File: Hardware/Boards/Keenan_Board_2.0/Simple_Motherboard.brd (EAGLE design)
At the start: 146.1 x 133.3 mm, 100 parts, among them U1 WIZ811MJ, U1_MUX 74HC4052D,653, U2_MUX 74HC4052D,653, U3_MUX 74HC4052D,653, U4_MUX 74HC4052D,653, U5_MUX 74HC4052D,653, U7_MUX 74HC4052D,653

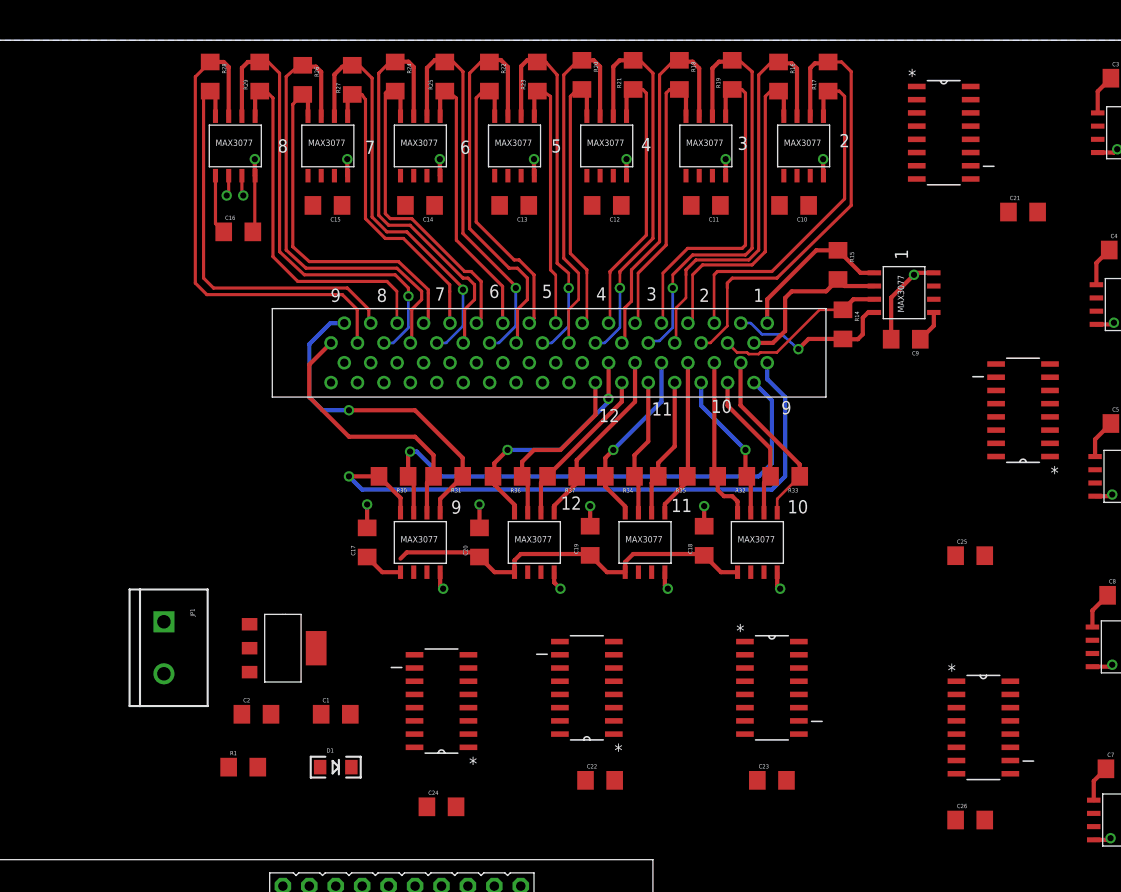
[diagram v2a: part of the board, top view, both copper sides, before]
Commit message: Routing power work
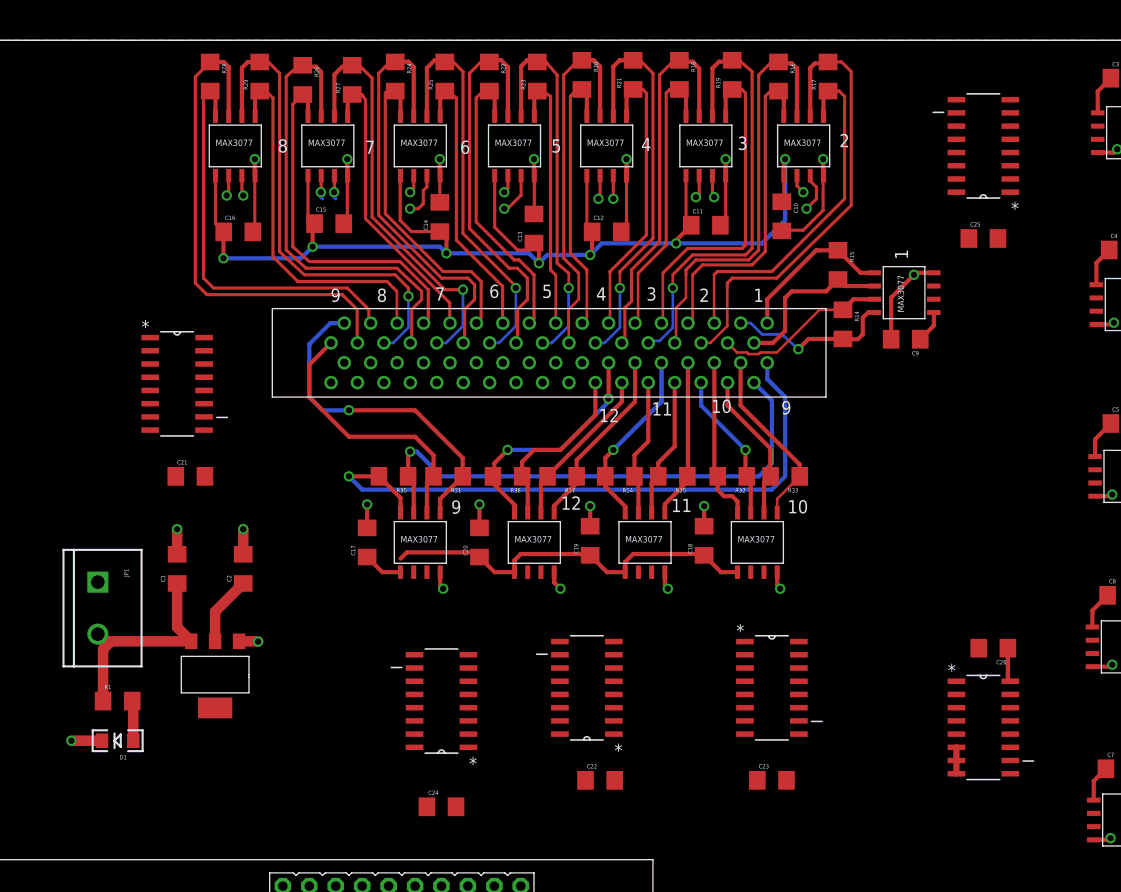
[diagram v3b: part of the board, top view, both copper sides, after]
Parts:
- moved C21 83.9 mm to (30.5, 91.4)
- moved U1_MUX 77.5 mm to (29.2, 100.3)
- moved C25 30.5 mm to (106.7, 114.3)
- moved U5_MUX 25.7 mm to (106.7, 123.2)
- moved D1 21.1 mm to (23.5, 66.0), turned to 180 degrees
- moved C1 20.7 mm to (29.2, 82.5), turned to 90 degrees
- moved C26 16.7 mm to (107.6, 74.9), turned to 180 degrees
- moved C2 14.0 mm to (35.6, 82.5), turned to 90 degrees
- moved R1 13.6 mm to (23.5, 69.8)
- moved JP1 7.41 mm to (21.6, 81.3)
- moved U$1 6.99 mm to (32.9, 72.4), turned to 180 degrees
- moved C13 2.93 mm to (63.5, 115.3), turned to 90 degrees
- moved C12 2.54 mm to (70.5, 114.9), turned to 0 degrees
- moved C14 2.21 mm to (54.5, 116.4), turned to 90 degrees
- moved C11 1.91 mm to (80.0, 115.6), turned to 0 degrees
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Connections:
- net +3V3: no longer R1.1
- net +5V: now also R1.1, U7_MUX.16
- net VCC: no longer U7_MUX.16
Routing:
- net +5V: track 72.1 -> 212.5 mm, vias 0 -> 7
- net GND: track 65.0 -> 108.1 mm, vias 28 -> 32
- net +3V3: track 0.00 -> 6.68 mm
- net RS485_6_TX: track 0.00 -> 4.31 mm, vias 0 -> 1
- net RS485_5_TX: track 0.00 -> 4.03 mm, vias 0 -> 1
- net N$45: track 0.00 -> 3.85 mm
- net RS485_2_TX: track 0.00 -> 3.82 mm, vias 0 -> 1
- net RS485_7_TX: track 0.00 -> 2.30 mm, vias 0 -> 1
- net RS485_7_RX: track 0.00 -> 2.30 mm, vias 0 -> 1
- net RS485_4_RX: track 0.00 -> 2.29 mm, vias 0 -> 1
- net RS485_4_TX: track 0.00 -> 2.22 mm, vias 0 -> 1
- net RS485_3_RX: track 0.00 -> 2.20 mm, vias 0 -> 1
- net RS485_3_TX: track 0.00 -> 2.13 mm, vias 0 -> 1
- net RS485_2_RX: track 0.00 -> 1.84 mm, vias 0 -> 1
- net RS485_5_RX: track 0.00 -> 1.73 mm, vias 0 -> 1
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
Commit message: More routing
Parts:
- moved C23 12.0 mm to (87.5, 74.1), turned to 180 degrees
- moved C21 11.9 mm to (30.8, 103.3), turned to 180 degrees
- moved U1_MUX 3.81 mm to (29.2, 96.5)
- moved U3_MUX 3.81 mm to (86.4, 67.3)
- moved C24 3.72 mm to (53.3, 63.2)
- moved C22 3.50 mm to (67.2, 64.5)
- moved C25 2.07 mm to (105.6, 116.0)
- moved C26 1.00 mm to (108.0, 74.0)
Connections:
- removed net VCC: U2_MUX.16, U3_MUX.16, U4_MUX.16, U5_MUX.16
- net +5V: now also U2_MUX.16, U3_MUX.16, U4_MUX.16, U5_MUX.16
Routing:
- net GND: track 108.1 -> 144.0 mm, vias 32 -> 44
- net +5V: track 212.5 -> 223.7 mm

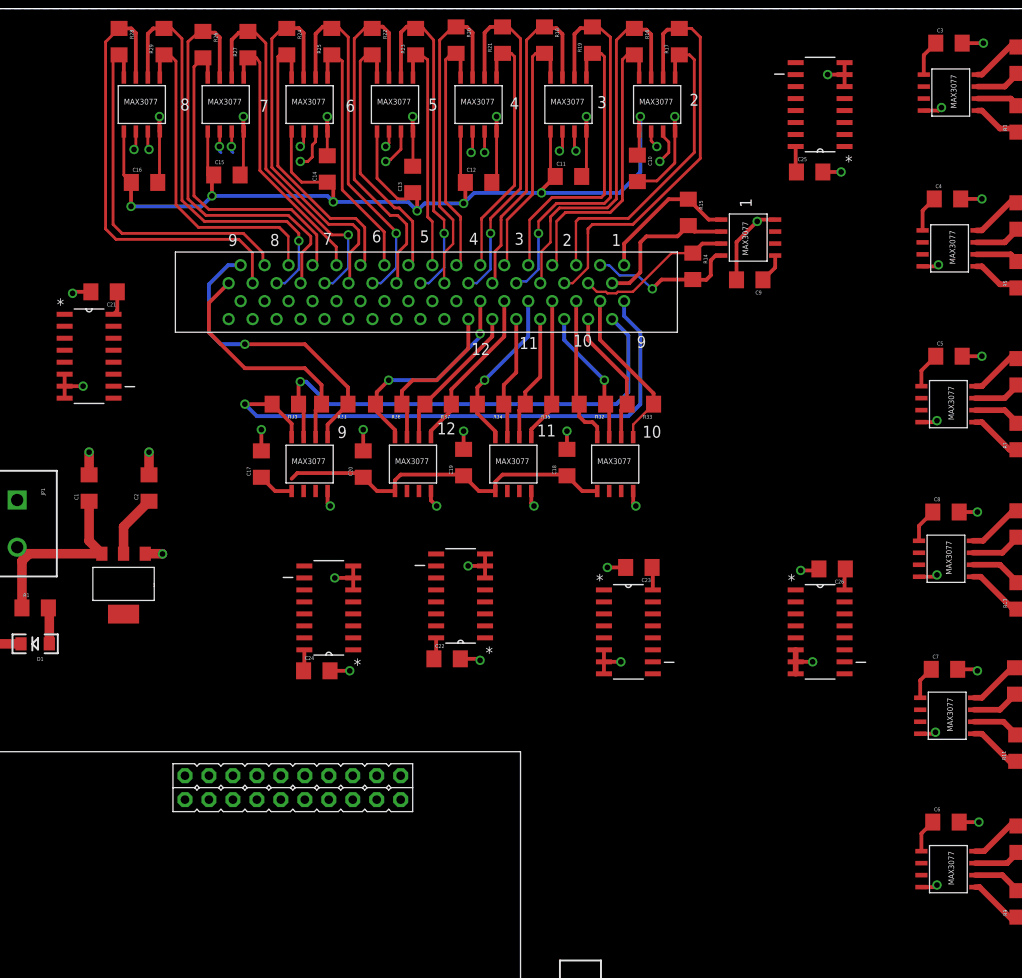
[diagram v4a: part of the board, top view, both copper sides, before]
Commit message: Routed some more mux stuff
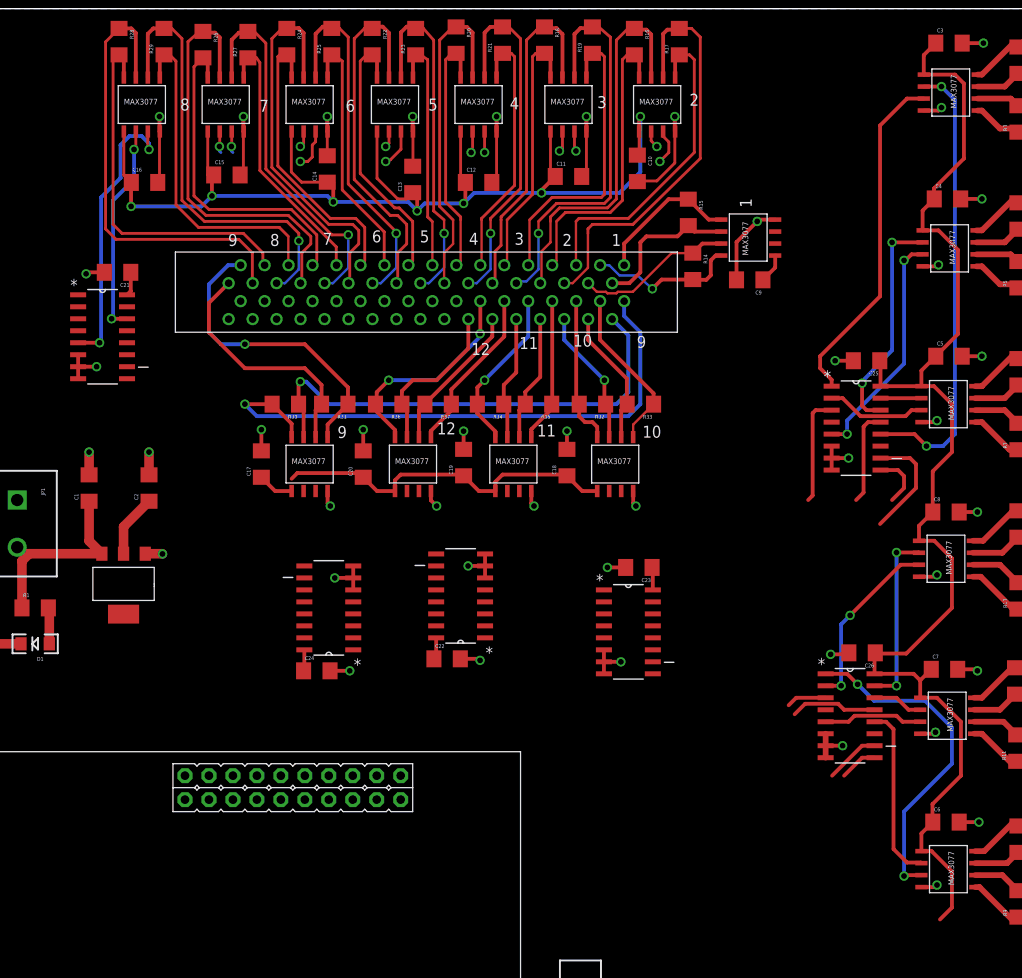
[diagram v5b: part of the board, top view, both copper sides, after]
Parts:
- moved U5_MUX 34.5 mm to (110.5, 88.9), turned to 0 degrees
- moved C25 20.9 mm to (111.6, 96.0), turned to 180 degrees
- moved C26 9.44 mm to (111.1, 65.1)
- moved U7_MUX 9.44 mm to (109.9, 58.4)
- moved C21 2.51 mm to (32.2, 105.4)
- moved U1_MUX 2.51 mm to (30.6, 98.6)
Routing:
- net +5V: track 223.7 -> 331.1 mm
- net RS485_13_RX: track 0.00 -> 48.2 mm, vias 0 -> 2
- net RS485_13_TX: track 0.00 -> 36.6 mm
- net RS485_16_TX: track 0.00 -> 35.5 mm, vias 0 -> 2
- net RS485_8_TX: track 1.96 -> 30.5 mm, vias 1 -> 2
- net RS485_14_TX: track 0.00 -> 24.8 mm, vias 0 -> 2
- net RS485_14_RX: track 0.00 -> 24.0 mm, vias 0 -> 2
- net RS485_8_RX: track 1.98 -> 22.5 mm, vias 1 -> 2
- net RS485_18_TX: track 0.00 -> 19.0 mm, vias 0 -> 2
- net RS485_18_RX: track 0.00 -> 18.9 mm, vias 0 -> 2
- net RS485_16_RX: track 0.00 -> 18.6 mm
- net U5_MUX_S0: track 0.00 -> 12.0 mm
- net U5TX: track 0.00 -> 11.5 mm
- net RS485_15_TX: track 0.00 -> 10.6 mm
- net RS485_17_TX: track 0.00 -> 10.5 mm
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
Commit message: Route city
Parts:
- moved S1 25.7 mm to (102.9, 40.6)
- moved U$2 16.6 mm to (25.4, 2.54)
- moved D1 13.8 mm to (32.5, 55.6)
- moved JP1 13.8 mm to (30.6, 70.8)
- moved U$1 13.8 mm to (41.9, 61.9)
- moved R1 13.8 mm to (32.5, 59.4)
- moved C1 13.8 mm to (38.3, 72.1)
- moved C2 13.8 mm to (44.6, 72.1)
- moved C23 12.7 mm to (90.3, 61.8), turned to 0 degrees
- moved U2_MUX 6.84 mm to (74.9, 68.6)
- moved C22 6.84 mm to (73.5, 61.9)
- moved U3_MUX 5.24 mm to (91.4, 68.6), turned to 180 degrees
- moved C18 5.08 mm to (84.9, 85.2)
- moved C19 5.08 mm to (74.0, 85.2)
- moved R15 5.08 mm to (97.8, 111.8)
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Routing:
- net RS485_5_RX: track 1.73 -> 132.2 mm, vias 1 -> 2
- net RS485_5_TX: track 4.03 -> 116.4 mm
- net RS485_1_TX: track 0.00 -> 105.1 mm, vias 0 -> 2
- net RS485_6_RX: track 1.73 -> 100.9 mm
- net RS485_6_TX: track 4.31 -> 101.8 mm
- net RS485_4_RX: track 2.29 -> 95.6 mm
- net RS485_1_RX: track 0.00 -> 91.0 mm, vias 0 -> 2
- net RS485_4_TX: track 2.22 -> 92.0 mm
- net RS485_7_TX: track 2.30 -> 87.4 mm
- net RS485_7_RX: track 2.30 -> 82.5 mm
- net RS485_3_RX: track 2.20 -> 81.3 mm
- net RS485_3_TX: track 2.13 -> 77.1 mm
- net RS485_2_RX: track 1.84 -> 65.2 mm
- net RS485_2_TX: track 3.82 -> 66.2 mm
- net +5V: track 331.1 -> 372.6 mm, vias 7 -> 13
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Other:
- board size 146.1 x 133.3 mm -> 120.7 x 133.3 mm
- board text removed: "Today, Tomorrow, Forever"

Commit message: All I do is route
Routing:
- net RS485_4_RX: track 95.6 -> 179.9 mm, vias 1 -> 2
- net RS485_4_TX: track 92.0 -> 163.5 mm, vias 1 -> 2
- net RS485_6_RX: track 100.9 -> 165.1 mm, vias 1 -> 2
- net RS485_6_TX: track 101.8 -> 160.8 mm, vias 1 -> 2
- net RS485_2_TX: track 66.2 -> 120.6 mm, vias 1 -> 2
- net RS485_2_RX: track 65.2 -> 112.7 mm, vias 1 -> 2
- net +5V: track 372.6 -> 419.1 mm
- net RS485_7_TX: track 87.4 -> 132.1 mm, vias 1 -> 2
- net RS485_7_RX: track 82.5 -> 121.4 mm, vias 1 -> 2
- net GND: track 144.7 -> 180.9 mm, vias 44 -> 48
- net RS485_3_RX: track 81.3 -> 113.4 mm, vias 1 -> 2
- net RS485_3_TX: track 77.1 -> 108.6 mm, vias 1 -> 2
- net RS485_10_RX: track 0.00 -> 31.0 mm, vias 0 -> 2
- net U5_MUX_S1: track 5.82 -> 33.1 mm
- net RS485_11_TX: track 0.00 -> 27.3 mm
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
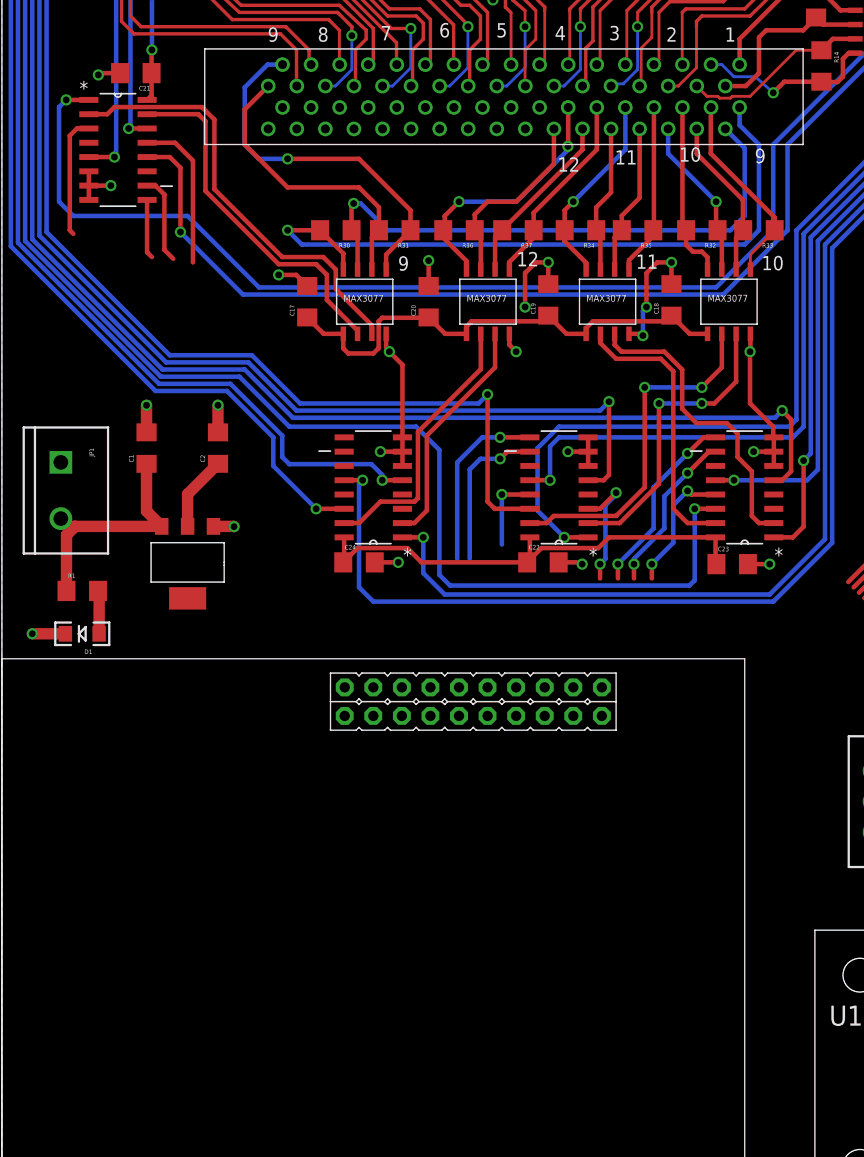
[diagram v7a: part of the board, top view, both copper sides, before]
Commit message: Basically just the breakout connections left
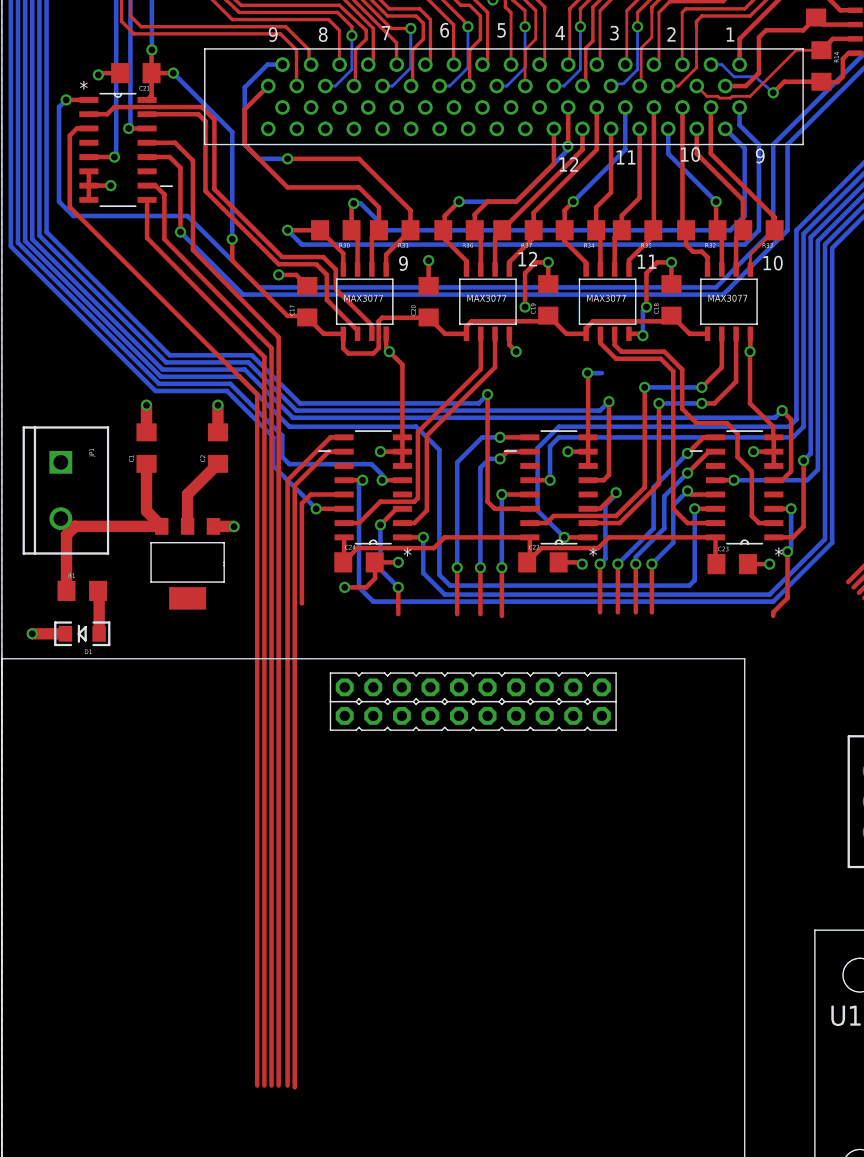
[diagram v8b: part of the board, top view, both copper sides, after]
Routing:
- net U1TX: track 10.8 -> 93.3 mm
- net U1_MUX_S1: track 5.26 -> 83.0 mm
- net U1_MUX_S0: track 7.91 -> 85.0 mm
- net U1RX: track 13.8 -> 90.1 mm
- net U4_MUX_S1: track 0.00 -> 60.4 mm
- net U4_MUX_S0: track 0.00 -> 59.1 mm
- net +5V: track 419.1 -> 448.7 mm, vias 13 -> 15
- net U4RX: track 0.00 -> 13.0 mm
- net U3TX: track 0.00 -> 11.7 mm, vias 0 -> 2
- net GND: track 180.9 -> 192.4 mm, vias 48 -> 50
- net U4TX: track 0.00 -> 11.1 mm, vias 0 -> 2
- net U2RX: track 6.93 -> 13.3 mm, vias 1 -> 2
- net U2_MUX_S1: track 16.0 -> 20.9 mm, vias 1 -> 2
- net U2_MUX_S0: track 13.9 -> 18.0 mm, vias 1 -> 2
- net U3_MUX_S1: track 16.8 -> 19.8 mm
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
